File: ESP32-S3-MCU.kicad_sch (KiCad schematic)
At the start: 38 parts, among them SW1 RESET, SW2 BOOT, U1 ESP32-S3FH4R2, X1 32.768KHz, Y1 40MHz

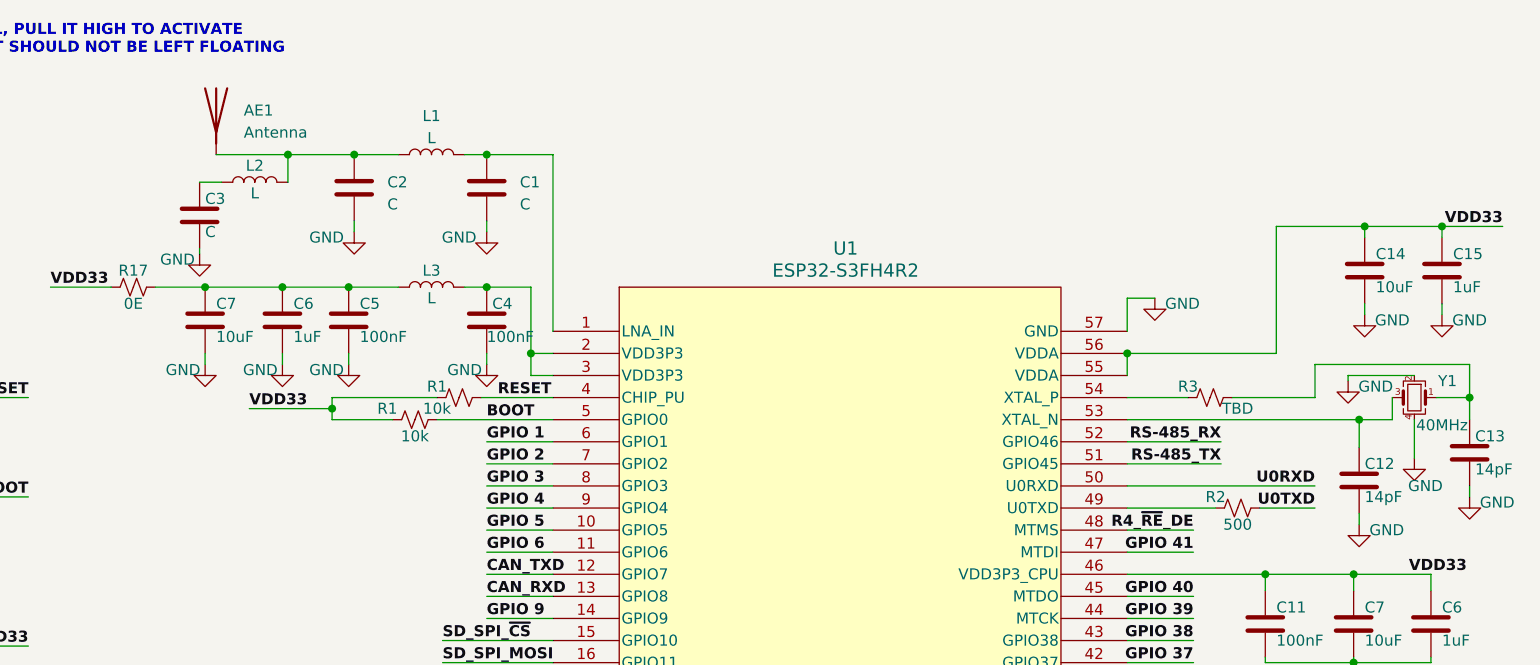
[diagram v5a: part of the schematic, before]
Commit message: Added LNA_IN Passives
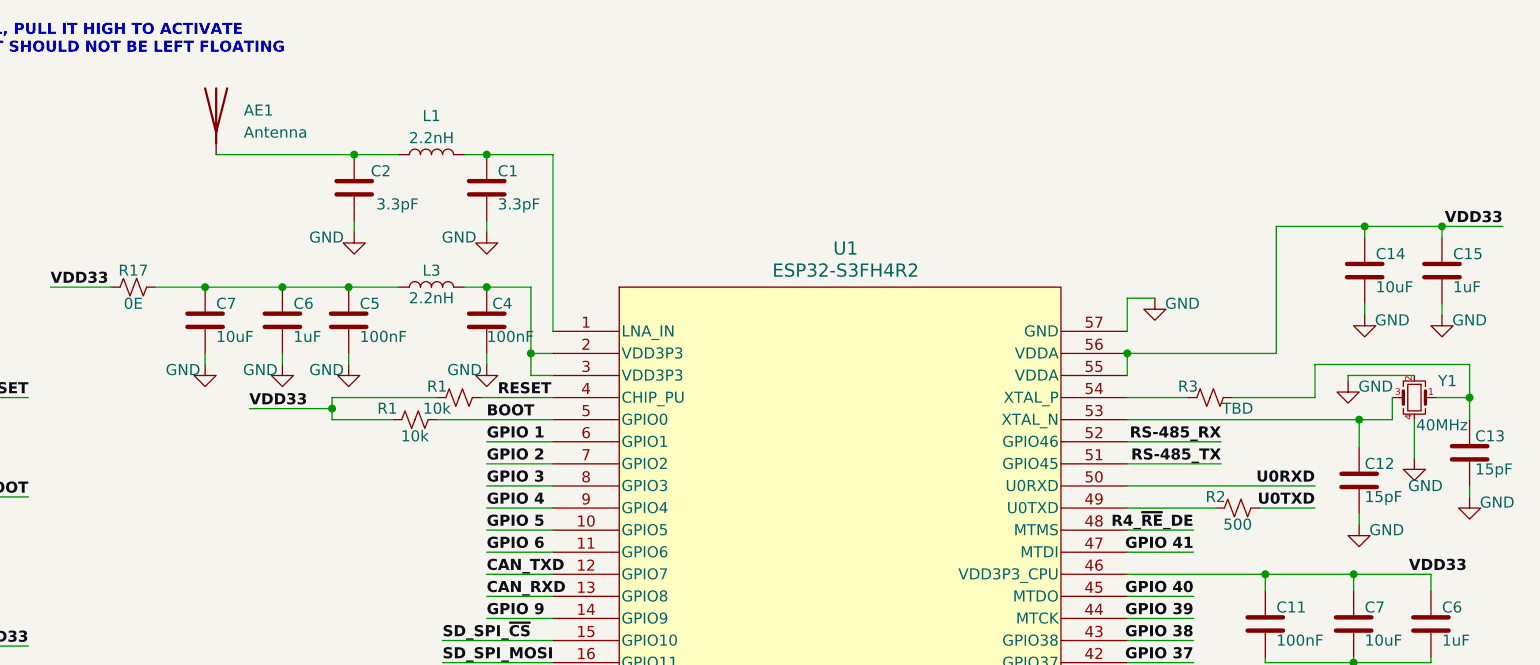
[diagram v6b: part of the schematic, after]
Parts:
- removed C3: C, symbol ESP32-S3_DB:C
- removed L2: L, symbol ESP32-S3_DB:L
- C1, C2: value C -> 3.3pF; footprint (none) -> ESP32-S3_Dev_Board:C_0402_1005Metric; PN (none) -> CC0402BRNPO9BN3R3
- C12, C13: value 14pF -> 15pF; footprint (none) -> ESP32-S3_Dev_Board:C_0402_1005Metric; PN (none) -> CC0402GRNPO8BN150
- C31, C32: footprint (none) -> ESP32-S3_Dev_Board:C_0402_1005Metric; PN (none) -> CC0402GRNPO8BN150
- L1: value L -> 2.2nH; footprint (none) -> ESP32-S3_Dev_Board:L_0402_1005Metric; PN (none) -> MLG1005S2N2CT000
- L3: value L -> 2.2nH; footprint (none) -> ESP32-S3_Dev_Board:L_0402_1005Metric; PN (none) -> MLK1005S2N2ST000
- R3: footprint (none) -> ESP32-S3_Dev_Board:R_0402_1005Metric; PN (none) -> RC0402FR-07270RL

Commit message: Instigated PCB Design
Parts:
- AE1: footprint (none) -> ESP32-S3_Dev_Board:BLE_ANTENNA
- L1: PN MLG1005S2N2CT000 -> MLK1005S2N2ST000
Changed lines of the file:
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@@
       (effects (font (size 1.27 1.27)) hide)
     )
-    (property "PN" "MLG1005S2N2CT000" (at 107.315 41.91 90)
+    (property "PN" "MLK1005S2N2ST000" (at 107.315 41.91 90)
       (effects (font (size 1.27 1.27)) hide)
     )
@@
   (symbol (lib_id "ESP32-S3_DB:C") (at 94.615 127.635 0) (unit 1)
     (in_bom yes) (on_board yes) (dnp no)
-    (property "Reference" "C31" (at 95.25 125.73 0)
+    (property "Reference" "C31" (at 90.805 125.73 0)
       (effects (font (size 1.27 1.27)) (justify left))
     )
@@
   (symbol (lib_id "ESP32-S3_DB:C") (at 109.22 127.635 0) (unit 1)
     (in_bom yes) (on_board yes) (dnp no)
-    (property "Reference" "C32" (at 105.41 125.73 0)
-      (effects (font (size 1.27 1.27)) (justify left))
-    )
-    (property "Value" "15pF" (at 104.14 129.54 0)
+    (property "Reference" "C32" (at 109.22 125.73 0)
+      (effects (font (size 1.27 1.27)) (justify left))
+    )
+    (property "Value" "15pF" (at 109.22 129.54 0)
       (effects (font (size 1.27 1.27)) (justify left))
     )
@@
       (effects (font (size 1.27 1.27)))
     )
-    (property "Value" "32.768KHz" (at 102.235 123.825 0)
+    (property "Value" "32.768KHz" (at 102.235 124.46 0)
       (effects (font (size 1.27 1.27)))
     )
@@
       (effects (font (size 1.27 1.27)) (justify left))
     )
-    (property "Footprint" "" (at 82.55 36.83 0)
+    (property "Footprint" "ESP32-S3_Dev_Board:BLE_ANTENNA" (at 82.55 36.83 0)
       (effects (font (size 1.27 1.27)) hide)
     )
@@
       (effects (font (size 1.27 1.27)) hide)
     )
+    (property "PN" "" (at 82.55 36.83 0)
+      (effects (font (size 1.27 1.27)) hide)
+    )

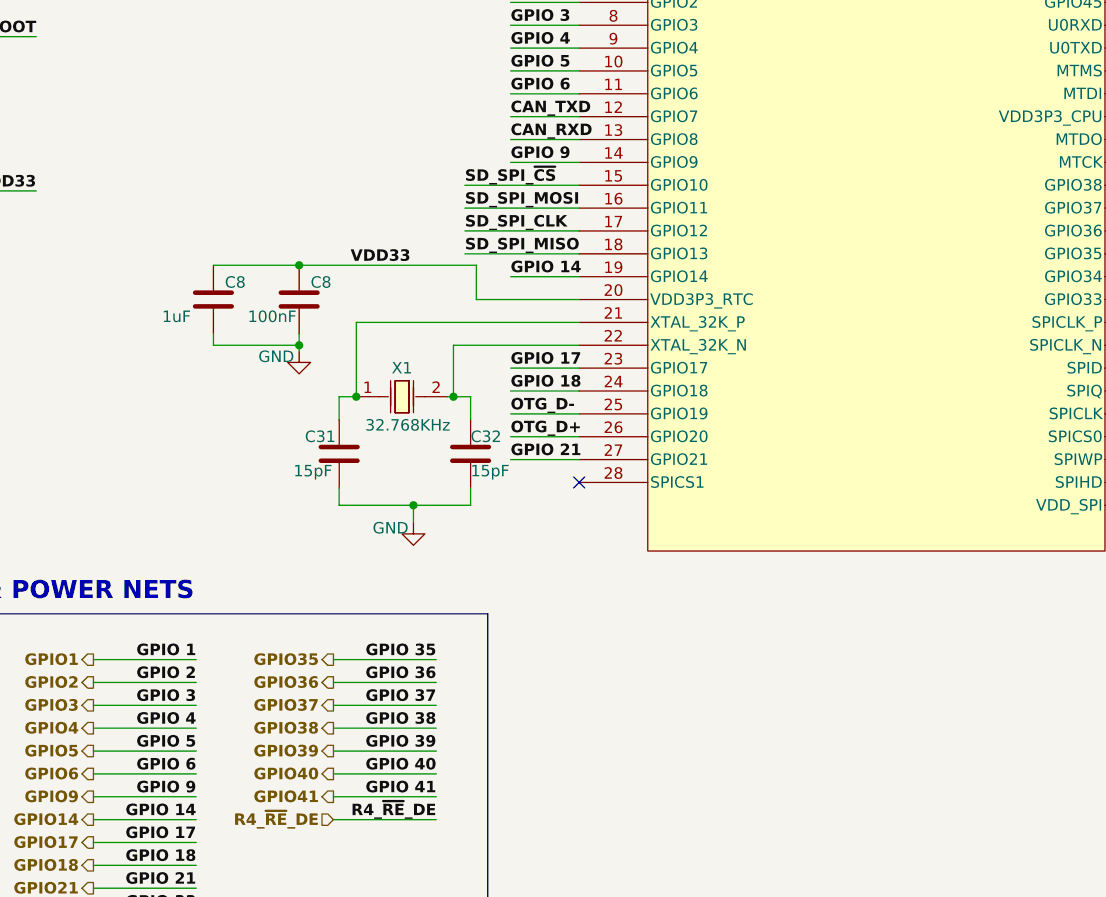
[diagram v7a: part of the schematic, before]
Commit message: Added bulk Decoupling and arranged components
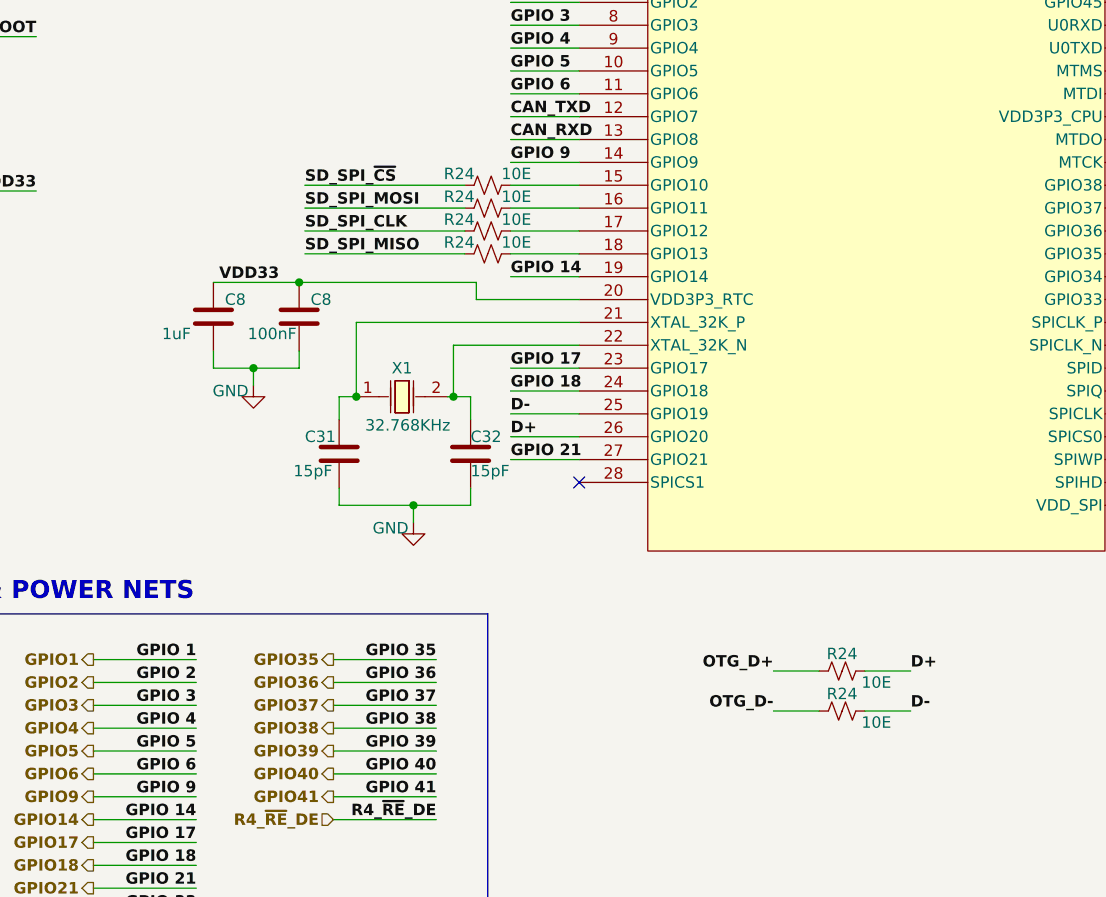
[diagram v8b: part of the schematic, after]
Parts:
- added R24 (x6): 10E, ESP32-S3_Dev_Board:R_0402_1005Metric, symbol ESP32-S3_DB:R_Small_US
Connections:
- net OTG_D+: now also R24.1; no longer U1.26 (GPIO20)
- net OTG_D-: now also R24.1; no longer U1.25 (GPIO19)
- net SD_CLK: now also R24.1; no longer U1.17 (GPIO12)
- net SD_MISO: now also R24.1; no longer U1.18 (GPIO13)
- net SD_MOSI: now also R24.1; no longer U1.16 (GPIO11)
- net SD_~{CS}: now also R24.1; no longer U1.15 (GPIO10)
- new net: R24.2, U1.17 (GPIO12)
- new net: R24.2, U1.16 (GPIO11)
- new net: R24.2, U1.15 (GPIO10)
- new net: R24.2, U1.18 (GPIO13)
- new net D+: R24.2, U1.26 (GPIO20)
- new net D-: R24.2, U1.25 (GPIO19)
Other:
- moved on the sheet: C8
